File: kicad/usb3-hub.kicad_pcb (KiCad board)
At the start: 6 copper layers, 70 x 140 mm, 215 parts, among them J1001 USB3_A, J101 DISPLAY, J102 USB3_B_Micro, J103 Barrel_Jack_Switch, J301 Debug, J302 Conn_01x03_Pin, J501 USB3_A, J601 USB3_A, J701 USB3_A, J801 USB3_A, J901 USB3_A, Q303 2N7002, SW1001 SW_Push, SW301 SW_Push, SW501 SW_Push, SW601 SW_Push, SW701 SW_Push, SW801 SW_Push, SW901 SW_Push, U1001 AP22804AW5, U201 USB5807, U301 W25Q16JVSS, U302 RP2040, U303 AP22804AW5, U401 TLV1117-33, U402 AP7363C-12E, U501 INA381A1, U502 AP22804AW5, U601 INA381A1, U602 AP22804AW5, U701 INA381A1, U702 AP22804AW5, U801 AP22804AW5, U901 AP22804AW5, Y201 25Mhz, Y301 12Mhz

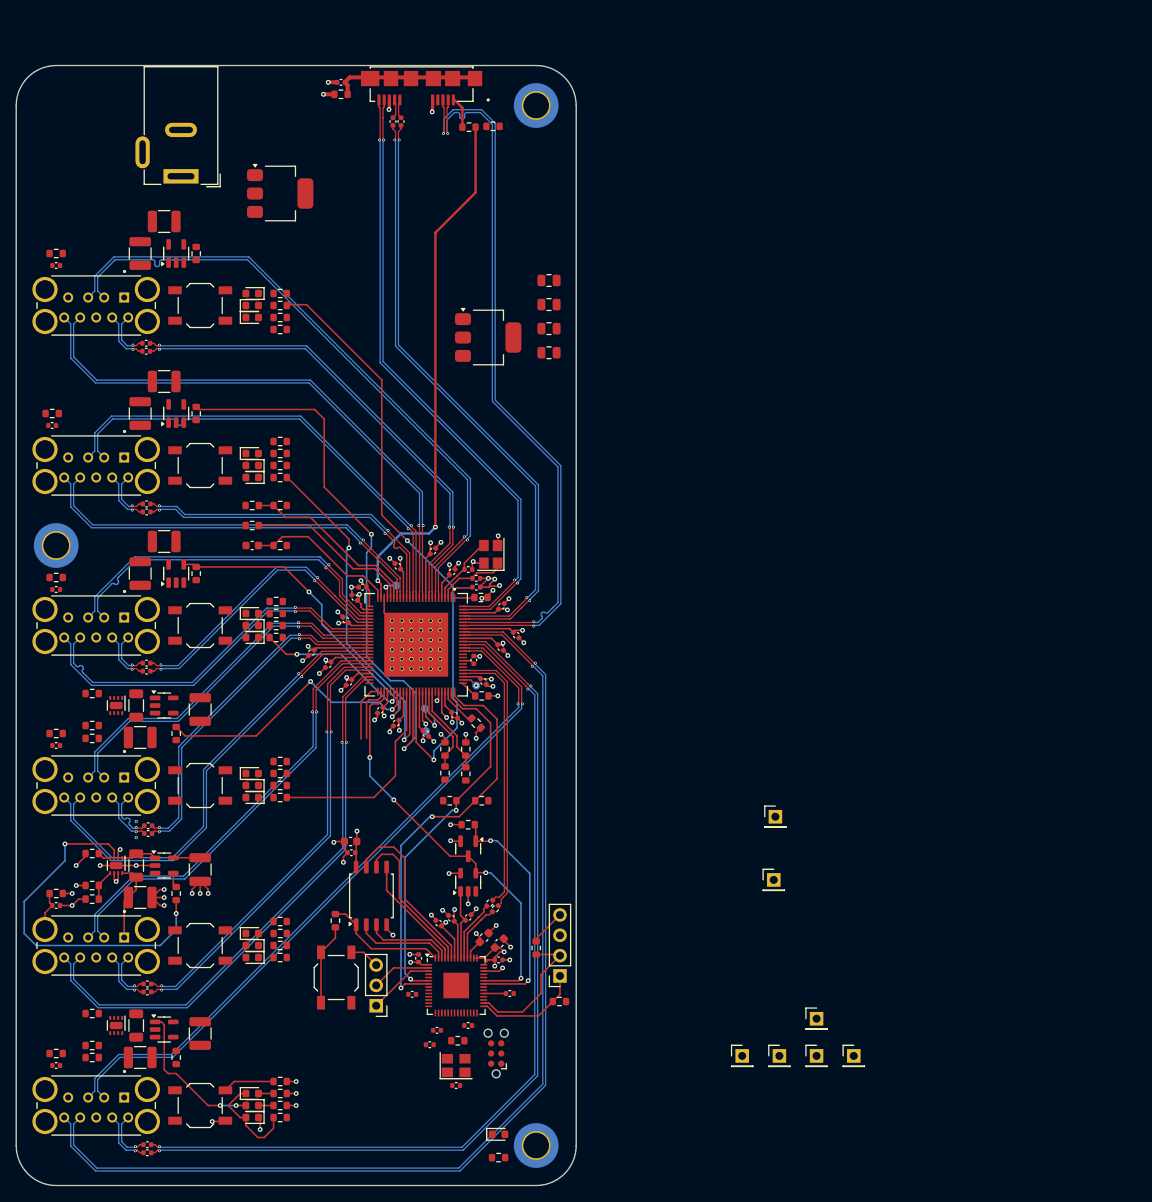
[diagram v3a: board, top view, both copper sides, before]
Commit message: Some more routing
rearranged the LED's
Exchanged the testpoints with a 1x5 connector.
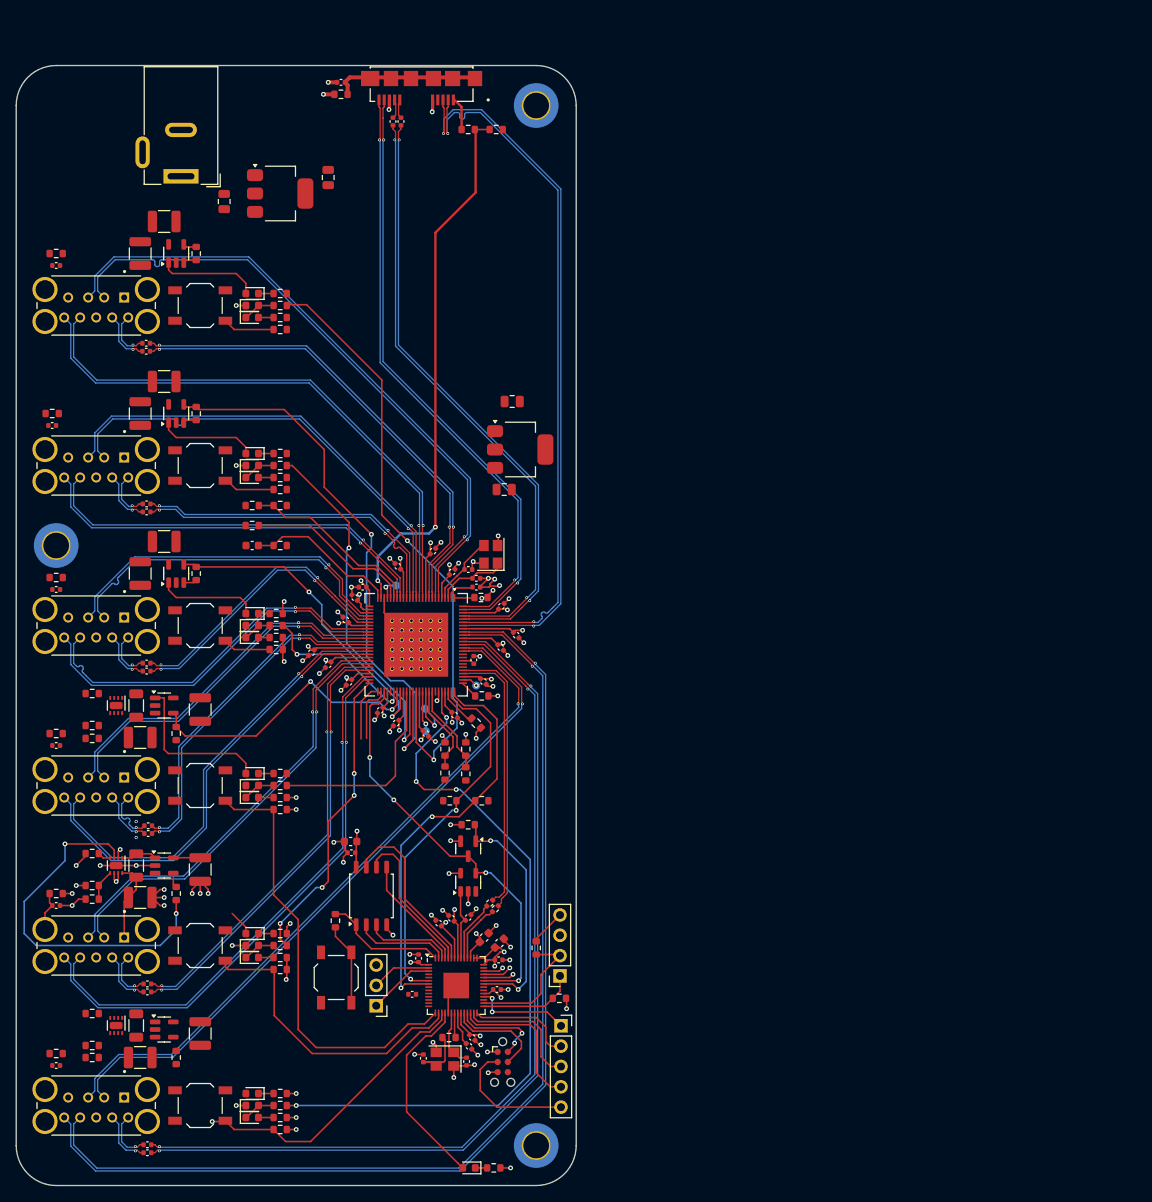
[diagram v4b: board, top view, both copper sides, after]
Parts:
- removed TP301, TP302, TP303, TP304, TP305, TP306, TP308: TestPoint, Connector_PinHeader_2.54mm:PinHeader_1x01_P2.54mm_Vertical
- added J303: Conn_01x05_Pin, Connector_PinSocket_2.54mm:PinSocket_1x05_P2.54mm_Vertical, F.Cu at (168.1, 155.0)
- moved C401 41.8 mm to (126.0, 52.0), turned to 90 degrees
- moved C402 31.8 mm to (139.0, 49.0), turned to 90 degrees
- moved C404 18.0 mm to (161.0, 88.0)
- moved U402 14.6 mm to (163.0, 83.0)
- moved C403 10.2 mm to (162.0, 77.0)
- moved R1006 6.00 mm to (132.5, 108.0)
- moved R512 6.00 mm to (133.0, 128.0)
- moved R612 6.00 mm to (133.0, 148.0)
- moved R712 6.00 mm to (133.0, 168.0)
- moved R906 6.00 mm to (133.0, 88.0)
- moved D301 5.60 mm to (156.6, 172.8), turned to 180 degrees
- moved C304 4.47 mm to (156.6, 157.6), turned to -45 degrees
- moved C315 3.27 mm to (156.3, 159.5), turned to -90 degrees
- moved D1002 3.00 mm to (129.5, 106.5)
- moved D502 3.00 mm to (129.5, 126.5)
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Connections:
- J301 pad 3: Net-(J301-~{RESET}) -> /Raspberry/~{RESET}
- R1006 pad 2: /TOGGLE6 -> /TOGGLE3
- R512 pad 2: /TOGGLE1 -> /TOGGLE4
- R612 pad 2: /TOGGLE2 -> /TOGGLE5
- R712 pad 2: /TOGGLE3 -> /TOGGLE6
- R806 pad 2: /TOGGLE4 -> /TOGGLE1
- R906 pad 2: /TOGGLE5 -> /TOGGLE2
- SW1001 pad 2: /TOGGLE6 -> /TOGGLE3
- SW501 pad 2: /TOGGLE1 -> /TOGGLE4
- SW601 pad 2: /TOGGLE2 -> /TOGGLE5
- SW701 pad 2: /TOGGLE3 -> /TOGGLE6
- SW801 pad 2: /TOGGLE4 -> /TOGGLE1
- SW901 pad 2: /TOGGLE5 -> /TOGGLE2
- U302 pad 26: Net-(U302-RUN) -> /Raspberry/RUN
- U302 pad 27: Net-(U302-GPIO16) -> /Raspberry/GPIO16
- U302 pad 28: unconnected-(U302-GPIO17-Pad28) -> /Raspberry/GPIO17
- U302 pad 31: Net-(U302-GPIO20) -> unconnected-(U302-GPIO20-Pad31)
- U302 pad 32: Net-(U302-GPIO21) -> /Raspberry/GPIO21
- U302 pad 5: Net-(U302-GPIO3) -> unconnected-(U302-GPIO3-Pad5)
- U302 pad 9: Net-(U302-GPIO7) -> unconnected-(U302-GPIO7-Pad9)
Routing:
- net /Hub/Port6.SPEED_IND: track 3.50 -> 90.2 mm, vias 1 -> 4
- net /TOGGLE4: track 0.00 -> 55.1 mm
- net /Hub/Port5.SPEED_IND: track 0.00 -> 38.2 mm, vias 0 -> 4
- net /TOGGLE5: track 0.00 -> 37.7 mm
- net /TOGGLE6: track 0.00 -> 36.8 mm, vias 0 -> 1
- net /Raspberry/STATUS_LED: track 0.00 -> 24.7 mm
- net /Port4/VBUS_HIGH: track 0.00 -> 19.8 mm
- net /Port6/VBUS_HIGH: track 19.0 -> 0.00 mm, vias 2 -> 0
- net /Raspberry/RUN: track 0.00 -> 18.6 mm
- net GND: track 95.1 -> 112.4 mm, vias 59 -> 72
- net /Raspberry/~{RESET}: track 0.00 -> 16.1 mm
- net /Raspberry/GPIO16: track 0.00 -> 16.0 mm
- net +3V3: track 77.4 -> 92.5 mm, vias 19 -> 26
- net /Raspberry/GPIO17: track 0.00 -> 13.3 mm
- net /Raspberry/SWCLK: track 0.00 -> 12.6 mm
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
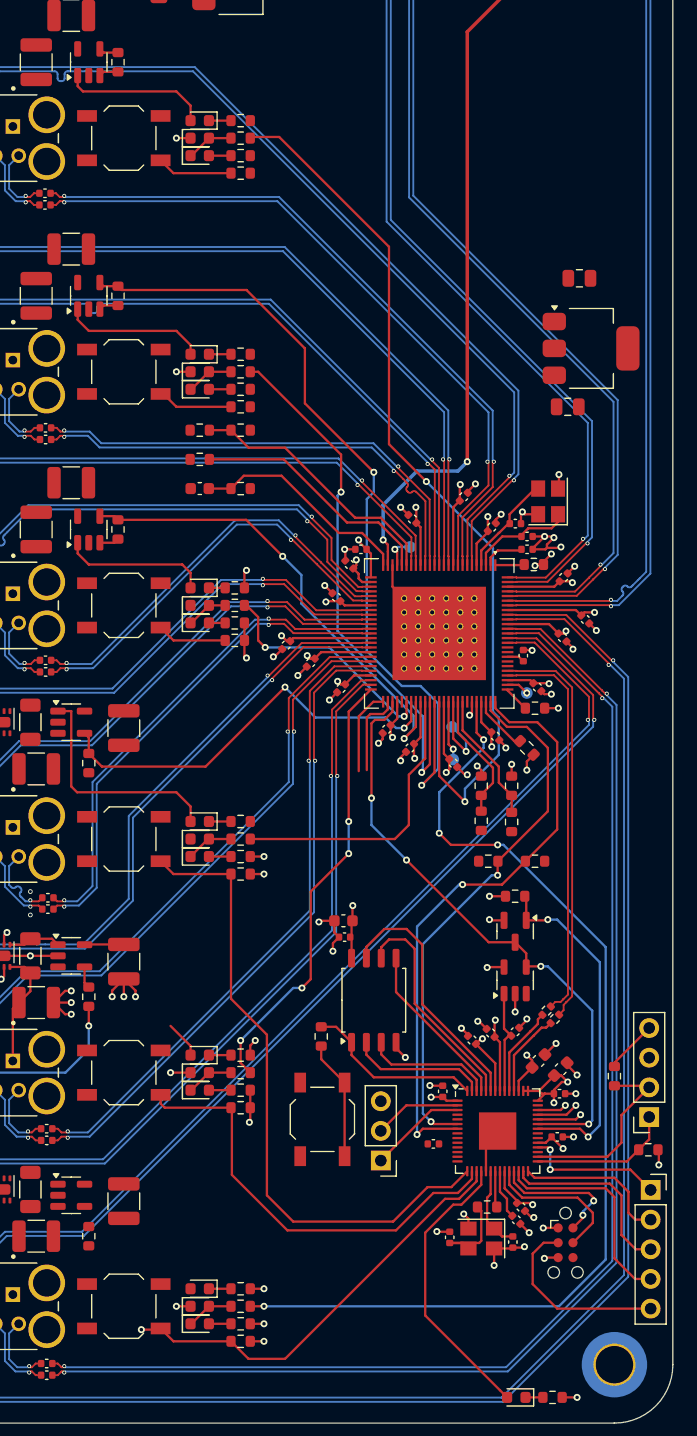
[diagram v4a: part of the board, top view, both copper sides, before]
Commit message: Replace 1.2V LDO with switching regulator
It just feels more reliable.
Also added 0R resistors between switch and alert signal. My hope is
that I can tell the switch to diable the port by pulling the
overcurrent low.
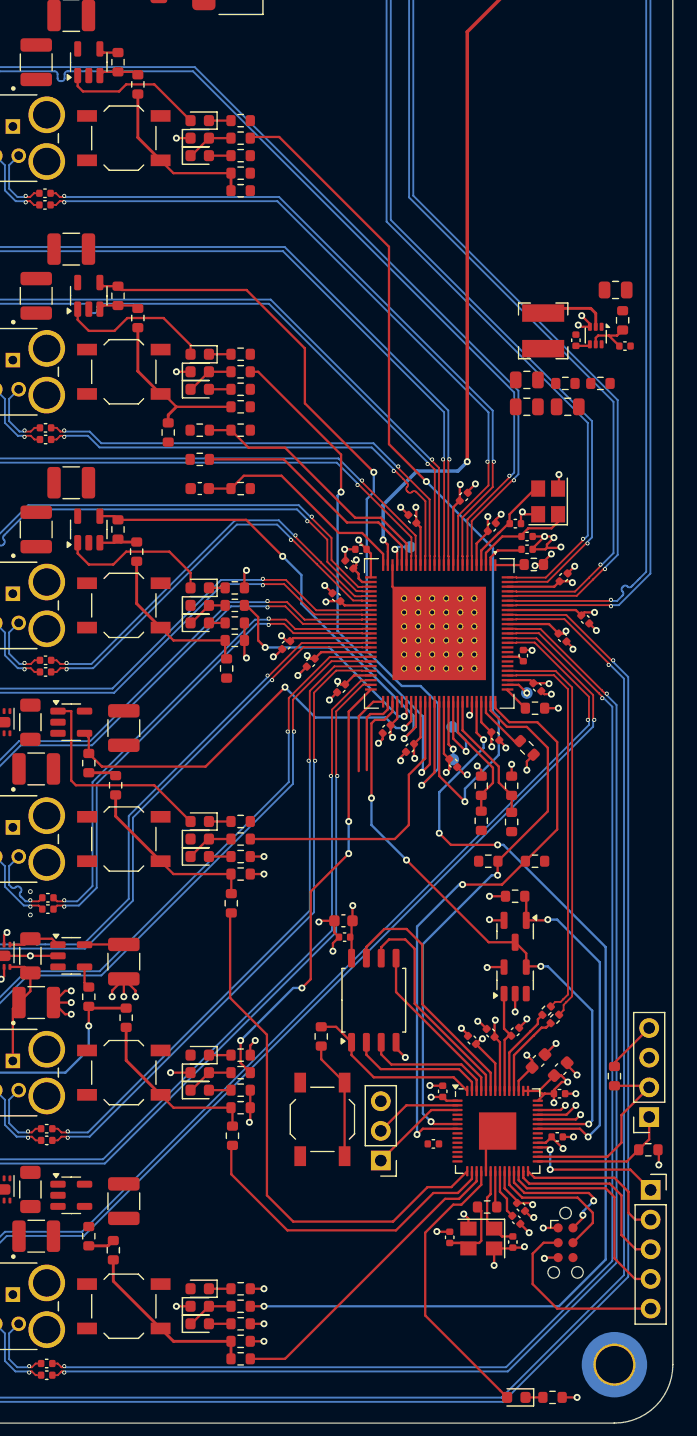
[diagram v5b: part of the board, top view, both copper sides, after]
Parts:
- added C405: 100nF, Capacitor_SMD:C_0402_1005Metric, F.Cu at (161.7, 82.3)
- added C406: 10uF, Capacitor_SMD:C_0805_2012Metric, F.Cu at (157.5, 88.0)
- added C407: 10uF, Capacitor_SMD:C_0805_2012Metric, F.Cu at (157.5, 85.7)
- added C408: 100nF, Capacitor_SMD:C_0402_1005Metric, F.Cu at (165.9, 82.8)
- added L401: 1uH 2.5A, Inductor_SMD:L_Bourns-SRN4018, F.Cu at (158.9, 81.5)
- added R1007: 0, Resistor_SMD:R_0603_1608Metric, F.Cu at (124.1, 100.4)
- added R1008: 0, Resistor_SMD:R_0603_1608Metric, F.Cu at (131.8, 110.4)
- added R401: 10k, Resistor_SMD:R_0603_1608Metric, F.Cu at (165.7, 80.6)
- added R402: 5.1k, Resistor_SMD:R_0603_1608Metric, F.Cu at (160.8, 86.0)
- added R403: 10k, Resistor_SMD:R_0603_1608Metric, F.Cu at (163.8, 86.0)
- added R502: 0, Resistor_SMD:R_0603_1608Metric, F.Cu at (122.3, 120.4)
- added R504: 0, Resistor_SMD:R_0603_1608Metric, F.Cu at (132.2, 130.5)
- added R602: 0, Resistor_SMD:R_0603_1608Metric, F.Cu at (123.2, 140.3)
- added R604: 0, Resistor_SMD:R_0603_1608Metric, F.Cu at (132.3, 150.4)
- added R702: 0, Resistor_SMD:R_0603_1608Metric, F.Cu at (122.1, 160.2)
- added R704: 0, Resistor_SMD:R_0603_1608Metric, F.Cu at (133.0, 169.5)
- added R807: 0, Resistor_SMD:R_0603_1608Metric, F.Cu at (124.2, 60.4)
- added R808: 0, Resistor_SMD:R_0603_1608Metric, F.Cu at (133.0, 69.5)
- added R907: 0, Resistor_SMD:R_0603_1608Metric, F.Cu at (124.2, 80.4)
- added R908: 0, Resistor_SMD:R_0603_1608Metric, F.Cu at (126.8, 90.2)
- U402: value AP7363C-12E -> AP62250Z6; footprint Package_TO_SOT_SMD:SOT-223-3_TabPin2 -> Package_TO_SOT_SMD:SOT-563
- moved C403 3.26 mm to (165.1, 78.0)
- moved U402 1.17 mm to (163.4, 81.9), turned to -90 degrees
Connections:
- R1006 pad 2: /TOGGLE3 -> Net-(R1006-Pad2)
- R512 pad 2: /TOGGLE4 -> Net-(R502-Pad2)
- R612 pad 2: /TOGGLE5 -> Net-(R602-Pad2)
- R712 pad 2: /TOGGLE6 -> Net-(R702-Pad2)
- R806 pad 2: /TOGGLE1 -> Net-(R806-Pad2)
- R906 pad 2: /TOGGLE2 -> Net-(R906-Pad2)
- SW1001 pad 2: /TOGGLE3 -> Net-(R1006-Pad2)
- SW501 pad 2: /TOGGLE4 -> Net-(R502-Pad2)
- SW601 pad 2: /TOGGLE5 -> Net-(R602-Pad2)
- SW701 pad 2: /TOGGLE6 -> Net-(R702-Pad2)
- SW801 pad 2: /TOGGLE1 -> Net-(R806-Pad2)
- SW901 pad 2: /TOGGLE2 -> Net-(R906-Pad2)
- U402 pad 2: GND -> Net-(U402-SW)
- U402 pad 3: +1V2 -> GND
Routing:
- net Net-(R702-Pad2): track 0.00 -> 15.1 mm
- net Net-(R502-Pad2): track 0.00 -> 15.0 mm
- net Net-(R602-Pad2): track 0.00 -> 14.7 mm
- net Net-(R906-Pad2): track 0.00 -> 14.6 mm
- net Net-(R806-Pad2): track 0.00 -> 14.5 mm
- net Net-(R1006-Pad2): track 0.00 -> 14.1 mm
- net /TOGGLE6: track 36.8 -> 26.7 mm, vias 1 -> 0
- net /TOGGLE5: track 37.7 -> 27.6 mm
- net /TOGGLE4: track 55.1 -> 45.4 mm
- net /TOGGLE1: track 6.48 -> 0.00 mm
- net /TOGGLE2: track 6.48 -> 0.00 mm
- net Net-(U402-SW): track 0.00 -> 5.99 mm
- net /TOGGLE3: track 5.98 -> 0.00 mm
- net Net-(U402-EN): track 0.00 -> 4.40 mm
- net /Port5/~{Alert}: track 44.9 -> 48.2 mm
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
